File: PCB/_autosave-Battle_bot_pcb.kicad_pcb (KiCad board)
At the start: 4 copper layers, 95.5 x 59.5 mm, 137 parts, among them J1 Conn_01x02, J2 USB_C_Receptacle_USB2.0_14P, J3 USB_C_Receptacle_USB2.0_14P, J4 Conn_01x03, J5 Conn_ARM_JTAG_SWD_10, J6 Conn_02x15_Counter_Clockwise, Q1 AO3401A, Q10 BSC026N08NS5, Q11 BSC026N08NS5, Q12 BSC026N08NS5, Q13 BSC026N08NS5, Q8 BSC026N08NS5, Q9 BSC026N08NS5, SW1 Reset, SW2 Boot, U1 LTC4412xS6, U10 ACS711xEXLT-31AB, U11 ACS711xEXLT-31AB, U12 STM32H743VITx, U2 USBLC6-2P6, U3 TPS62172DSG, U4 LSM6DS3, U5 ESP32-S3, U6 USBLC6-2P6, U7 TPS2116DRL, U9 FAN7388, Y3 25MHz, Y4 40MHz

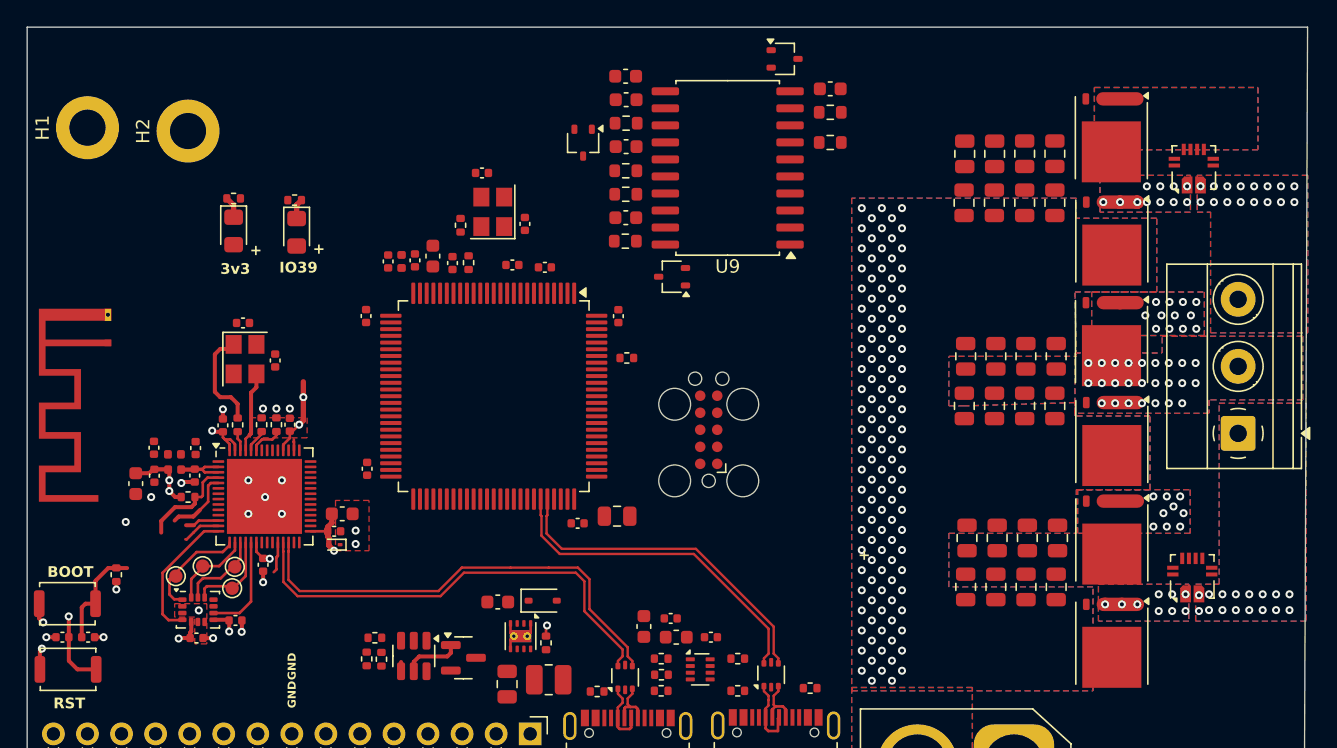
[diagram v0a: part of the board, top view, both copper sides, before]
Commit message: Hardware updates: STM32H7 and Inverted design
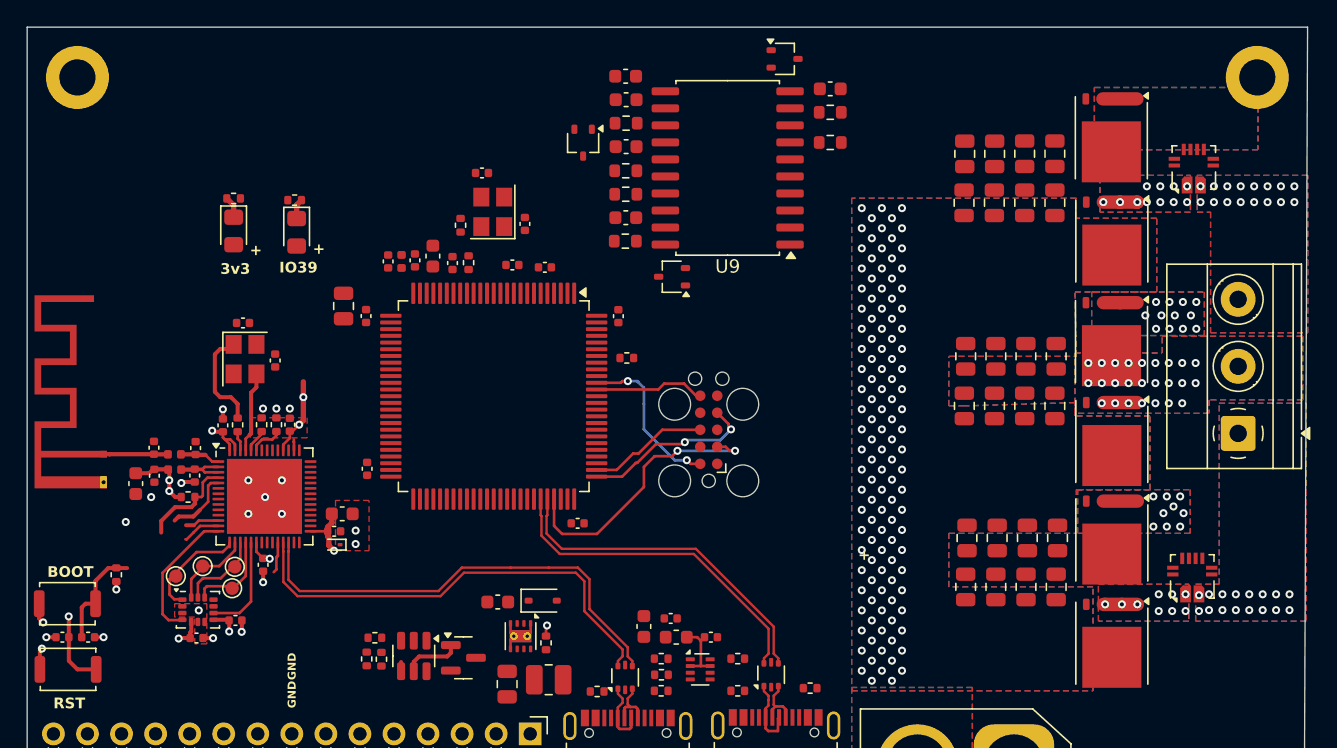
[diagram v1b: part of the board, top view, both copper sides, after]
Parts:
- AE1: footprint RF_Antenna:Texas_SWRA117D_2.4GHz_Left -> RF_Antenna:Texas_SWRA117D_2.4GHz_Right
- moved H2 79.9 mm to (196.8, 89.2)
- moved C87 25.7 mm to (128.6, 106.3), turned to 90 degrees
- moved AE1 8.31 mm to (110.7, 117.3)
- moved H1 3.82 mm to (108.8, 89.2)
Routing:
- net Net-(J5-SWDIO/TMS): track 0.00 -> 20.6 mm, vias 0 -> 2
- net Net-(J5-SWCLK/TCK): track 0.00 -> 13.2 mm, vias 0 -> 2
- net Net-(J5-~{RESET}): track 0.00 -> 12.1 mm, vias 0 -> 2
- net Net-(J5-NC/TDI): track 0.00 -> 8.97 mm
- net Net-(J5-SWO/TDO): track 0.00 -> 8.28 mm
- net VBUS: track 0.00 -> 4.90 mm
- net Net-(AE1-A): track 0.00 -> 4.81 mm
- net Net-(U5-LNA_IN/RF): track 0.00 -> 3.02 mm

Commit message: Latest PCB version
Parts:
- removed C54: 10u, Capacitor_SMD:C_0603_1608Metric
- removed C58: 1u, Capacitor_SMD:C_0603_1608Metric
- removed C68, C72, C73: 4.7u, Capacitor_SMD:C_0603_1608Metric
- removed R4: 100k, Resistor_SMD:R_0402_1005Metric
- added C30: 75p, Capacitor_SMD:C_0402_1005Metric, F.Cu at (132.3, 111.2)
- added C31: 100n, Capacitor_SMD:C_0402_1005Metric, F.Cu at (118.0, 84.3)
- added C8: 100n, Capacitor_SMD:C_0402_1005Metric, F.Cu at (130.9, 113.8)
- added C88: 2.2u, Capacitor_SMD:C_0603_1608Metric, F.Cu at (128.8, 101.0)
- added C89: 2.2u, Capacitor_SMD:C_0603_1608Metric, F.Cu at (147.2, 106.2)
- added C9: 22u, Capacitor_SMD:C_0805_2012Metric, F.Cu at (128.2, 116.0)
- added C90: 100n, Capacitor_SMD:C_0402_1005Metric, F.Cu at (241.5, 81.7)
- added C91: 100n, Capacitor_SMD:C_0402_1005Metric, F.Cu at (242.3, 86.8)
- added C92: 100n, Capacitor_SMD:C_0402_1005Metric, F.Cu at (190.2, 98.7)
- added C93: 1u, Capacitor_SMD:C_0402_1005Metric, F.Cu at (190.2, 100.7)
- added C94: 100n, Capacitor_SMD:C_0402_1005Metric, F.Cu at (194.5, 116.9)
- added C95: 1u, Capacitor_SMD:C_0402_1005Metric, F.Cu at (205.4, 118.0)
- added C96: 100n, Capacitor_SMD:C_0402_1005Metric, F.Cu at (194.4, 123.3)
- added C97: 1u, Capacitor_SMD:C_0402_1005Metric, F.Cu at (210.9, 125.7)
- added D11: SZESD9B5.0ST5G, Diode_SMD:D_SOD-923, F.Cu at (148.2, 103.2)
- added D12: SZESD9B5.0ST5G, Diode_SMD:D_SOD-923, F.Cu at (148.8, 108.0)
- added D13: SZESD9B5.0ST5G, Diode_SMD:D_SOD-923, F.Cu at (148.0, 96.8)
- added D5: LED, LED_SMD:LED_0805_2012Metric_Pad1.15x1.40mm_HandSolder, F.Cu at (154.4, 83.3)
- added D6: SZESD9B5.0ST5G, Diode_SMD:D_SOD-923, F.Cu at (160.2, 100.2)
- added D7: SZESD9B5.0ST5G, Diode_SMD:D_SOD-923, F.Cu at (147.8, 89.7)
- added H3: MountingHole, MountingHole:MountingHole_2.7mm_M2.5_DIN965_Pad, F.Cu at (173.5, 126.0)
- added H4: MountingHole, MountingHole:MountingHole_2.7mm_M2.5_DIN965_Pad, F.Cu at (107.5, 126.0)
- added J7: Conn_01x04, Connector_PinHeader_2.54mm:PinHeader_1x04_P2.54mm_Horizontal, F.Cu at (129.9, 74.4)
- added J8: Conn_01x04, Connector_PinHeader_2.54mm:PinHeader_1x04_P2.54mm_Horizontal, F.Cu at (141.3, 74.4)
- added J9: Conn_02x10_Counter_Clockwise, Connector_PinHeader_2.54mm:PinHeader_2x11_P2.54mm_Vertical, F.Cu at (115.1, 127.9)
- added R27: 1k, Resistor_SMD:R_0402_1005Metric, F.Cu at (154.4, 80.8)
- added R28: 100k, Resistor_SMD:R_0402_1005Metric, F.Cu at (133.4, 111.2)
- added R29: 49.9, Resistor_SMD:R_0402_1005Metric, F.Cu at (136.7, 111.2)
- added R30: 22.1k, Resistor_SMD:R_0402_1005Metric, F.Cu at (134.5, 111.2)
- added R31: 511k, Resistor_SMD:R_0402_1005Metric, F.Cu at (131.1, 111.2)
- added R32: 105k, Resistor_SMD:R_0402_1005Metric, F.Cu at (130.0, 111.2)
- added R33: 2k, Resistor_SMD:R_0402_1005Metric, F.Cu at (135.7, 111.2)
- added R34: 50k, Resistor_SMD:R_0402_1005Metric, F.Cu at (122.9, 85.2)
- added R35: 50k, Resistor_SMD:R_0402_1005Metric, F.Cu at (118.0, 85.4)
- added R36: 10k, Resistor_SMD:R_0402_1005Metric, F.Cu at (122.9, 84.1)
- added R38: 50k, Resistor_SMD:R_0402_1005Metric, F.Cu at (114.2, 85.1)
- added R39: 50k, Resistor_SMD:R_0402_1005Metric, F.Cu at (111.7, 73.0)
- added R40: 50k, Resistor_SMD:R_0402_1005Metric, F.Cu at (114.2, 84.1)
- added SW3: SW_DPDT_x2, Button_Switch_SMD:SW_SPDT_PCM12, F.Cu at (155.3, 73.6)
- added U13: IR2103, Package_SO:SOIC-8_3.9x4.9mm_P1.27mm, F.Cu at (200.5, 124.7)
- added U14: ACS725xLCTR-50AB, Package_SO:SOIC-8_3.9x4.9mm_P1.27mm, F.Cu at (207.8, 71.1)
- added U8: IR2103, Package_SO:SOIC-8_3.9x4.9mm_P1.27mm, F.Cu at (200.2, 108.1)
- C1: value 10u -> 4.7u
- C10, C13: value 3.3p -> 2.2p
- D10, D8, D9: value BAS16W -> 1N5819WS; footprint Package_TO_SOT_SMD:SOT-323_SC-70 -> Diode_SMD:D_SOD-323
- J1: footprint Connector_AMASS:AMASS_XT60-F_1x02_P7.20mm_Vertical -> Connector_AMASS:AMASS_XT60-M_1x02_P7.20mm_Vertical
- J5: value Conn_ARM_JTAG_SWD_10 -> Micro_SD_Card_Det1; footprint Connector:Tag-Connect_TC2050-IDC-FP_2x05_P1.27mm_Vertical -> Connector_Card:microSD_HC_Hirose_DM3D-SF
- J6: value Conn_02x15_Counter_Clockwise -> TC2030; footprint Connector_PinHeader_2.54mm:PinHeader_2x15_P2.54mm_Horizontal -> Connector:Tag-Connect_TC2030-IDC-FP_2x03_P1.27mm_Vertical
- L2: value 2.2u -> 10u; footprint Inductor_SMD:L_1008_2520Metric -> Inductor_SMD:L_APV_APH0420
- L3: value 2.2n -> 2.6n
- R20, R22, R23, R24, R25: value 10 -> 100; footprint Resistor_SMD:R_0603_1608Metric -> Resistor_SMD:R_0805_2012Metric
- R21: footprint Resistor_SMD:R_0603_1608Metric -> Resistor_SMD:R_0805_2012Metric
- U3: value TPS62172DSG -> TPS54308; footprint Package_SON:WSON-8-1EP_2x2mm_P0.5mm_EP0.9x1.6mm_ThermalVias -> Package_TO_SOT_SMD:SOT-23-6
- U9: value FAN7388 -> IR2103; footprint Package_SO:SOIC-20W_7.5x12.8mm_P1.27mm -> Package_SO:SOIC-8_3.9x4.9mm_P1.27mm
- moved D9 67.4 mm to (206.8, 124.2), turned to 0 degrees
- moved C77 62.1 mm to (199.4, 69.2), turned to 0 degrees
- moved R21 61.9 mm to (210.2, 110.9)
- moved R22 61.9 mm to (210.7, 102.7)
- moved R23 61.2 mm to (210.7, 99.7)
- moved R20 60.9 mm to (210.3, 107.1)
- moved D10 60.0 mm to (206.8, 127.1)
- moved C51 58.4 mm to (186.0, 69.2), turned to 0 degrees
- moved J1 57.8 mm to (172.2, 83.0), turned to -90 degrees
- moved C69 54.3 mm to (194.9, 72.3), turned to 0 degrees
- moved J5 53.1 mm to (119.2, 77.1), turned to 0 degrees
- moved Q8 50.4 mm to (229.8, 106.7), turned to 180 degrees
- moved C55 50.2 mm to (186.0, 78.3), turned to 0 degrees
- moved C62 49.1 mm to (190.5, 75.3), turned to 0 degrees
- moved Q10 48.8 mm to (229.8, 95.1), turned to 180 degrees
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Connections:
- net /Inverter/FAULT_U renamed /Inverter motor controller/FAULT_U
- net /Inverter/IA renamed /Inverter motor controller/IA
- net /Inverter/IC renamed /Inverter motor controller/IC
- net /Inverter/VI_U renamed /Inverter motor controller/VI_U
- net /Inverter/VI_V renamed /Inverter motor controller/VI_V
- C25 pad 1: Net-(U12-NRST) -> /STM32-H7/NRST
- D10 pad 1: +BATT -> Net-(D10-K)
- D10 pad 2: unconnected-(D10-NC-Pad2) -> +BATT
- D8 pad 1: +BATT -> Net-(D8-K)
- D8 pad 2: unconnected-(D8-NC-Pad2) -> +BATT
- D9 pad 1: +BATT -> Net-(D9-K)
- D9 pad 2: unconnected-(D9-NC-Pad2) -> +BATT
- J4 pad 2: /Inverter/IB -> /Inverter motor controller/IB
- J5 pad 1: +3.3V -> Net-(J5-DAT2)
- J5 pad 10: Net-(J5-~{RESET}) -> GND
- J5 pad 2: Net-(J5-SWDIO/TMS) -> /SD-Card/SD_CS
- J5 pad 3: GND -> /SD-Card/SD_MOSI
- J5 pad 4: Net-(J5-SWCLK/TCK) -> +3.3V
- J5 pad 5: GND -> /SD-Card/SD_SCLK
- J5 pad 6: Net-(J5-SWO/TDO) -> GND
- J5 pad 7: unconnected-(J5-KEY-Pad7) -> /SD-Card/SD_MISO
- J5 pad 8: Net-(J5-NC/TDI) -> Net-(J5-DAT1)
- J5 pad 9: GND -> /SD-Card/SD_DET
- J6 pad 1: unconnected-(J6-Pin_1-Pad1) -> +3.3V
- J6 pad 2: unconnected-(J6-Pin_2-Pad2) -> /STM32-H7/SWDIO
- J6 pad 3: unconnected-(J6-Pin_3-Pad3) -> /STM32-H7/NRST
- J6 pad 4: unconnected-(J6-Pin_4-Pad4) -> /STM32-H7/SWCLK
- J6 pad 5: unconnected-(J6-Pin_5-Pad5) -> GND
- J6 pad 6: unconnected-(J6-Pin_6-Pad6) -> /STM32-H7/SWO/TDO
- Q10 pad 1: /Inverter/IB -> /Inverter motor controller/IB
- Q10 pad 2: /Inverter/IB -> /Inverter motor controller/IB
- Q10 pad 3: /Inverter/IB -> /Inverter motor controller/IB
- Q11 pad 5: /Inverter/IB -> /Inverter motor controller/IB
- Q12 pad 1: /Inverter/VS3 -> /Inverter motor controller/VS3
- Q12 pad 2: /Inverter/VS3 -> /Inverter motor controller/VS3
- Q12 pad 3: /Inverter/VS3 -> /Inverter motor controller/VS3
- Q13 pad 5: /Inverter/VS3 -> /Inverter motor controller/VS3
- Q8 pad 1: /Inverter/VS1 -> /Inverter motor controller/VS1
- Q8 pad 2: /Inverter/VS1 -> /Inverter motor controller/VS1
- Q8 pad 3: /Inverter/VS1 -> /Inverter motor controller/VS1
- Q9 pad 5: /Inverter/VS1 -> /Inverter motor controller/VS1
- R20 pad 1: /Inverter/Q1 -> /Inverter motor controller/Q1
- R21 pad 1: /Inverter/Q4 -> /Inverter motor controller/Q4
- R22 pad 1: /Inverter/Q6 -> /Inverter motor controller/Q6
- R23 pad 1: /Inverter/Q3 -> /Inverter motor controller/Q3
- R24 pad 1: /Inverter/Q5 -> /Inverter motor controller/Q5
- R25 pad 1: /Inverter/Q2 -> /Inverter motor controller/Q2
- U10 pad 1: /Inverter/VS1 -> /Inverter motor controller/VS1
- U10 pad 10: unconnected-(U10-VCC-Pad10) -> +3.3V
- U11 pad 1: /Inverter/VS3 -> /Inverter motor controller/VS3
- U11 pad 10: unconnected-(U11-VCC-Pad10) -> +3.3V
- U11 pad 4: /Inverter/FAULT_V -> +3.3V
- U12 pad 14: Net-(U12-NRST) -> /STM32-H7/NRST
- U12 pad 28: unconnected-(U12-PA4-Pad28) -> /ESP32/CS
- U12 pad 29: unconnected-(U12-PA5-Pad29) -> /ESP32/SCLK
- U12 pad 30: unconnected-(U12-PA6-Pad30) -> /ESP32/MISO
- U12 pad 31: unconnected-(U12-PA7-Pad31) -> /ESP32/MOSI
- U12 pad 48: unconnected-(U12-VCAP-Pad48) -> Net-(C88-Pad1)
- U12 pad 68: unconnected-(U12-PA9-Pad68) -> Net-(D5-A)
- U12 pad 72: Net-(J5-SWDIO/TMS) -> /STM32-H7/SWDIO
- U12 pad 73: unconnected-(U12-VCAP-Pad73) -> Net-(C89-Pad1)
- U12 pad 76: Net-(J5-SWCLK/TCK) -> /STM32-H7/SWCLK
- U12 pad 77: Net-(J5-NC/TDI) -> unconnected-(U12-PA15-Pad77)
- U12 pad 81: unconnected-(U12-PD0-Pad81) -> /STM32-H7/HIN3
- U12 pad 82: unconnected-(U12-PD1-Pad82) -> /STM32-H7/LIN3
- U12 pad 83: unconnected-(U12-PD2-Pad83) -> /Inverter motor controller/HIN2
- U12 pad 84: unconnected-(U12-PD3-Pad84) -> /Inverter motor controller/LIN2
- U12 pad 85: unconnected-(U12-PD4-Pad85) -> /Inverter motor controller/HIN1
- U12 pad 86: unconnected-(U12-PD5-Pad86) -> /Inverter motor controller/LIN1
- U12 pad 89: Net-(J5-SWO/TDO) -> /STM32-H7/SWO/TDO
- U12 pad 90: Net-(J5-~{RESET}) -> unconnected-(U12-PB4-Pad90)
- U3 pad 2: /USB/LOAD -> Net-(U3-SW)
- U3 pad 4: GND -> Net-(U3-FB)
- U3 pad 5: GND -> Net-(U3-EN)
- U3 pad 6: +3.3V -> Net-(U3-BOOT)
- U5 pad 38: unconnected-(U5-GPIO33-Pad38) -> /ESP32/MOSI
- U5 pad 39: unconnected-(U5-GPIO34-Pad39) -> /ESP32/MISO
- U5 pad 40: unconnected-(U5-GPIO35-Pad40) -> /ESP32/SCLK
- U5 pad 41: unconnected-(U5-GPIO36-Pad41) -> /ESP32/CS
- U9 pad 1: /Inverter/HIN1 -> +BATT
- U9 pad 2: /Inverter/LIN1 -> /Inverter motor controller/HIN2
- U9 pad 3: /Inverter/HIN2 -> /Inverter motor controller/LIN2
- U9 pad 4: /Inverter/LIN2 -> GND
- U9 pad 5: /Inverter/HIN3 -> /Inverter motor controller/Q6
- U9 pad 6: /Inverter/LIN3 -> /Inverter motor controller/IB
- U9 pad 7: /Inverter/Q2 -> /Inverter motor controller/Q3
- U9 pad 8: /Inverter/VS3 -> Net-(D9-K)
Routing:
- net /ESP32/ESP_USB_D+: track 34.5 -> 5.52 mm
- net /ESP32/ESP_USB_D-: track 34.5 -> 5.83 mm
- net /STM32-H7/NRST: track 0.00 -> 27.9 mm
- net /STM32-H7/SWDIO: track 0.00 -> 26.5 mm
- net Net-(J5-SWDIO/TMS): track 20.6 -> 0.00 mm, vias 2 -> 0
- net /USB/V_USB_STM: track 0.00 -> 18.8 mm
- net +5V: track 0.00 -> 18.0 mm, vias 0 -> 2
- net /ESP32/CS: track 6.63 -> 22.3 mm
- net /ESP32/SCLK: track 0.00 -> 15.6 mm
- net /SD-Card/SD_DET: track 0.00 -> 15.5 mm
- net /ESP32/MISO: track 0.00 -> 15.3 mm
- net /USB/LOAD: track 0.00 -> 15.3 mm
- net /ESP32/MOSI: track 0.00 -> 15.1 mm
- net /STM32-H7/SWCLK: track 0.00 -> 13.6 mm
- net Net-(J5-SWCLK/TCK): track 13.2 -> 0.00 mm, vias 2 -> 0
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- added copper zone on F.Cu, net /USB/LOAD
- removed copper zone on B.Cu, net +BATT
- removed copper zone on In1.Cu, net +BATT
- removed copper zone on In2.Cu, net +BATT
- removed copper zone on B.Cu, net /Inverter motor controller/IA
- removed copper zone on F.Cu, net /Inverter motor controller/IA
- removed copper zone on In1.Cu, net /Inverter motor controller/IA
- removed copper zone on In2.Cu, net /Inverter motor controller/IA
- removed copper zone on B.Cu, net /Inverter motor controller/IC
- removed copper zone on F.Cu, net /Inverter motor controller/IC
- removed copper zone on In1.Cu, net /Inverter motor controller/IC
- removed copper zone on In2.Cu, net /Inverter motor controller/IC
- removed copper zone on B.Cu, net /Inverter/IB
- removed copper zone on F.Cu, net /Inverter/IB
- removed copper zone on In1.Cu, net /Inverter/IB
- removed copper zone on In2.Cu, net /Inverter/IB
- removed copper zone on B.Cu, net /Inverter/VS1
- removed copper zone on F.Cu, net /Inverter/VS1
- removed copper zone on In1.Cu, net /Inverter/VS1
- removed copper zone on In2.Cu, net /Inverter/VS1
- removed copper zone on B.Cu, net /Inverter/VS3
- removed copper zone on F.Cu, net /Inverter/VS3
- removed copper zone on In1.Cu, net /Inverter/VS3
- removed copper zone on In2.Cu, net /Inverter/VS3
- removed copper zone on B.Cu, net GND
- removed copper zone on In1.Cu, net GND
- removed copper zone on In2.Cu, net GND
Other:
- board size 95.5 x 59.5 mm -> 73.5 x 59.5 mm
- board text added: "ESP"
- board text added: "FD CAN 1"
- board text added: "FD CAN 2"
- board text added: "RX"
- board text added: "STM"
- board text added: "STM BOOT MODE"
- board text added: "TX"
- board text removed: "+"
- board text removed: "IO39"
